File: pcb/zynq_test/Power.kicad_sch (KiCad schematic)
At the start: 83 parts, among them J1401 Barrel_Jack, J1402 Conn_02x04_Odd_Even, Q1104 2N7002E, SW1401 Enable, U1401 LM65645RZT, U1402 LM65645RZT, U1403 LM65645RZT, U1404 LM65645RZT, U1405 74LVC1G17, U1406 TPS259470x

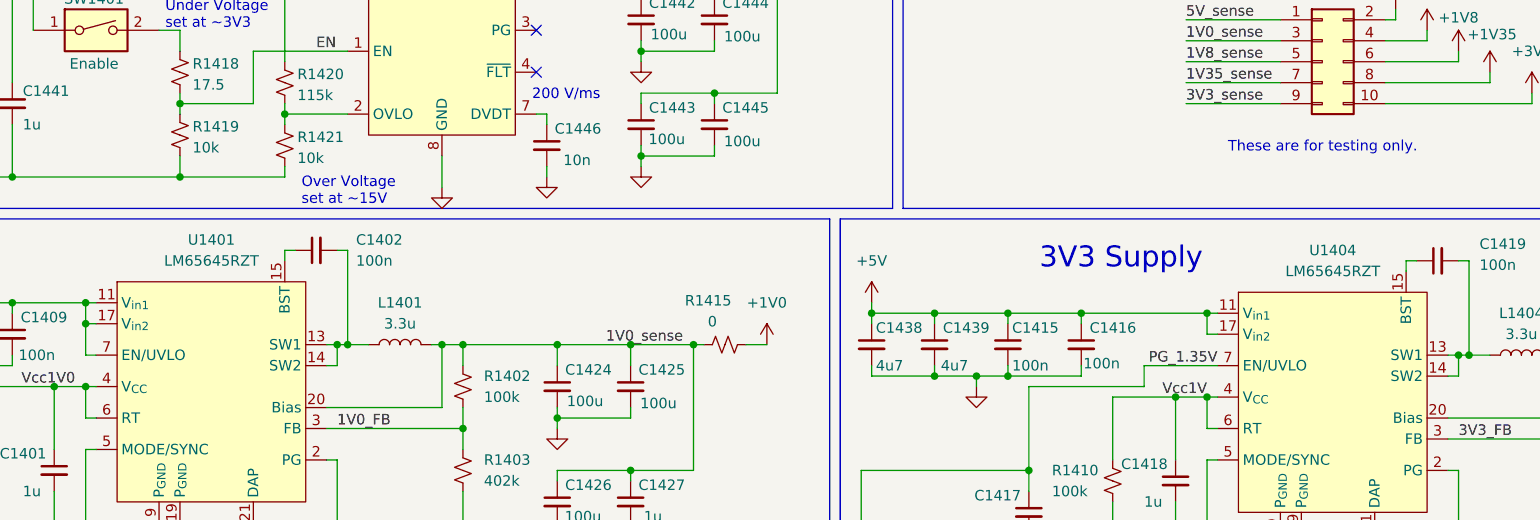
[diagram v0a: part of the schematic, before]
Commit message: Finished most of the schematic, will start routing soon
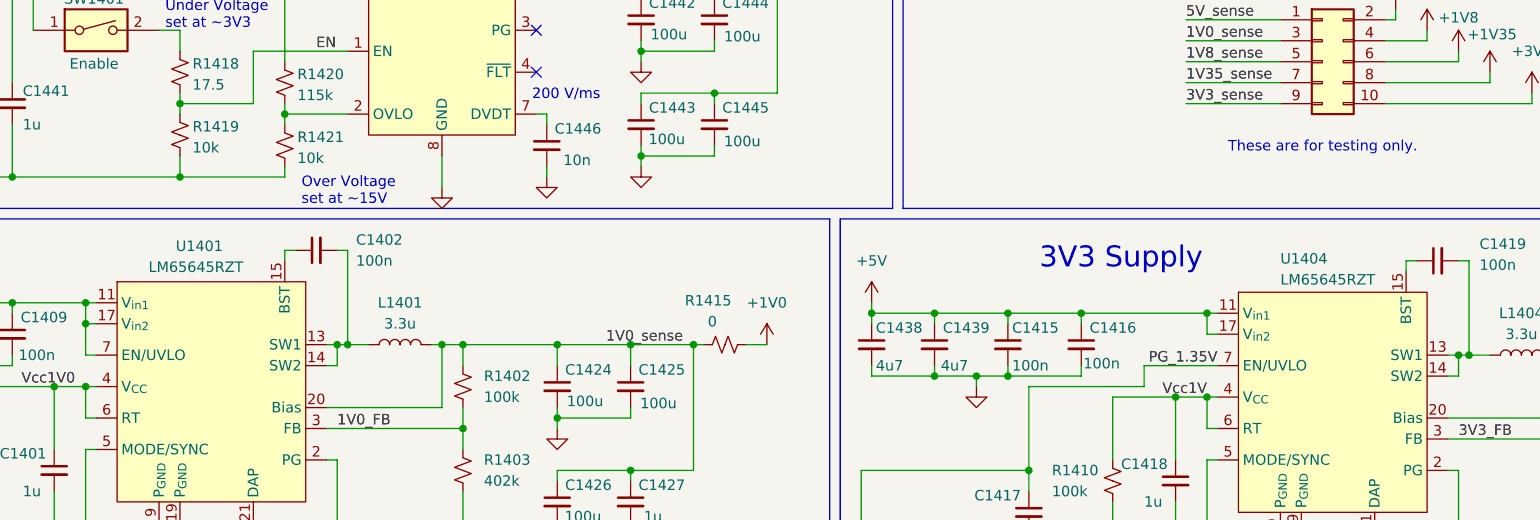
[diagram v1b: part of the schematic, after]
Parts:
- J1401: footprint (none) -> Connector_BarrelJack:BarrelJack_GCT_DCJ200-10-A_Horizontal
- J1402: value Conn_02x04_Odd_Even -> Conn_02x05_Odd_Even; footprint (none) -> Connector_PinSocket_2.54mm:PinSocket_2x05_P2.54mm_Horizontal
- U1405: footprint (none) -> Package_TO_SOT_SMD:Texas_R-PDSO-G5_DCK-5; True values (none) -> SN74LVC1G17DCKR
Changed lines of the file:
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@@
 		(on_board yes)
 		(dnp no)
-		(fields_autoplaced yes)
 		(property "Reference" "U1404"
-			(at 210.82 53.34 0)
-			(effects
-				(font
-					(size 1.27 1.27)
-				)
+			(at 204.47 54.356 0)
+			(effects
+				(font
+					(size 1.27 1.27)
+				)
+				(justify left)
 			)
 		)
 		(property "Value" "LM65645RZT"
-			(at 210.82 55.88 0)
-			(effects
-				(font
-					(size 1.27 1.27)
-				)
+			(at 204.47 56.896 0)
+			(effects
+				(font
+					(size 1.27 1.27)
+				)
+				(justify left)
 			)
 		)
@@
 			)
 		)
-		(property "Footprint" ""
+		(property "Footprint" "Package_TO_SOT_SMD:Texas_R-PDSO-G5_DCK-5"
 			(at 208.28 110.49 0)
 			(effects
@@
 		)
 		(property "Description" "Single Schmitt Buffer Gate, Low-Voltage CMOS"
+			(at 210.82 110.49 0)
+			(effects
+				(font
+					(size 1.27 1.27)
+				)
+				(hide yes)
+			)
+		)
+		(property "True values" "SN74LVC1G17DCKR"
 			(at 210.82 110.49 0)
 			(effects
@@
 		(on_board yes)
 		(dnp no)
-		(fields_autoplaced yes)
 		(property "Reference" "U1401"
-			(at 74.93 52.07 0)
-			(effects
-				(font
-					(size 1.27 1.27)
-				)
+			(at 70.612 52.832 0)
+			(effects
+				(font
+					(size 1.27 1.27)
+				)
+				(justify left)
 			)
 		)
 		(property "Value" "LM65645RZT"
-			(at 74.93 54.61 0)
-			(effects
-				(font
-					(size 1.27 1.27)
-				)
+			(at 67.31 55.372 0)
+			(effects
+				(font
+					(size 1.27 1.27)
+				)
+				(justify left)
 			)
 		)
@@
 			)
 		)
-		(property "Value" "Conn_02x04_Odd_Even"
+		(property "Value" "Conn_02x05_Odd_Even"
 			(at 211.582 22.86 0)
 			(effects
@@
 			)
 		)
-		(property "Footprint" ""
+		(property "Footprint" "Connector_PinSocket_2.54mm:PinSocket_2x05_P2.54mm_Horizontal"
 			(at 209.55 30.48 0)
 			(effects
@@
 			)
 		)
-		(property "Footprint" ""
+		(property "Footprint" "Connector_BarrelJack:BarrelJack_GCT_DCJ200-10-A_Horizontal"
 			(at 38.1 25.146 0)
 			(effects

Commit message: Almost done with BOM
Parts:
- removed R1413, R1414: 0, symbol Device:R_Small_US
- removed SW1401: Enable, symbol Switch:SW_DIP_x01
- added C1447, C1448, C1449, C1450: 10pf, Capacitor_SMD:C_0402_1005Metric, symbol Device:C_Small
- added C1451: 100u, Capacitor_SMD:C_1210_3225Metric, symbol Device:C_Small
- added C1452, C1453, C1454, C1455, C1456: 2.2n, Capacitor_SMD:C_0402_1005Metric, symbol Device:C_Small
- added R1414: 787R, Resistor_SMD:R_0402_1005Metric, symbol Device:R_US
- added R1416: 1k, Resistor_SMD:R_0402_1005Metric, symbol Device:R_Small_US
- added SW1401: Enable, Button_Switch_THT:SW_Slide-03_Wuerth-WS-SLTV_10x2.5x6.4_P2.54mm, symbol Switch:SW_SPDT_321
- C1401: renamed from C1434; footprint (none) -> Capacitor_SMD:C_0805_2012Metric
- C1402: renamed from C1436; footprint (none) -> Capacitor_SMD:C_0805_2012Metric
- C1403: renamed from C1432; footprint (none) -> Capacitor_SMD:C_0805_2012Metric
- C1404: renamed from C1435; footprint (none) -> Capacitor_SMD:C_0805_2012Metric
- C1405: renamed from C1437; footprint (none) -> Capacitor_SMD:C_0805_2012Metric
- C1406: renamed from C1433; footprint (none) -> Capacitor_SMD:C_0805_2012Metric
- C1407: renamed from C1411; footprint (none) -> Capacitor_SMD:C_0402_1005Metric
- C1408: renamed from C1413; footprint (none) -> Capacitor_SMD:C_0402_1005Metric
- C1409: renamed from C1410; footprint (none) -> Capacitor_SMD:C_0402_1005Metric
- C1410: renamed from C1408; footprint (none) -> Capacitor_SMD:C_0402_1005Metric
- C1411: renamed from C1412; footprint (none) -> Capacitor_SMD:C_0402_1005Metric
- C1412: renamed from C1407; footprint (none) -> Capacitor_SMD:C_0402_1005Metric
- C1413: renamed from C1414; footprint (none) -> Capacitor_SMD:C_0402_1005Metric
- C1414: renamed from C1441; footprint (none) -> Capacitor_SMD:C_0805_2012Metric
- C1415: renamed from C1409; footprint (none) -> Capacitor_SMD:C_0402_1005Metric
- C1416: renamed from C1401; footprint (none) -> Capacitor_SMD:C_0805_2012Metric
- C1417: renamed from C1405; footprint (none) -> Capacitor_SMD:C_0805_2012Metric
- C1418: renamed from C1403; footprint (none) -> Capacitor_SMD:C_0805_2012Metric
- C1419: renamed from C1402; footprint (none) -> Capacitor_SMD:C_0402_1005Metric
- C1420: renamed from C1406; footprint (none) -> Capacitor_SMD:C_0402_1005Metric
- C1421: renamed from C1404; footprint (none) -> Capacitor_SMD:C_0402_1005Metric
- C1422: renamed from C1446; footprint (none) -> Capacitor_SMD:C_0402_1005Metric
- C1423: renamed from C1424; footprint (none) -> Capacitor_SMD:C_1210_3225Metric
- C1424: renamed from C1426; footprint (none) -> Capacitor_SMD:C_1210_3225Metric
- C1425: renamed from C1420; footprint (none) -> Capacitor_SMD:C_0805_2012Metric
- C1426: renamed from C1425; value 100u -> 1u; footprint (none) -> Capacitor_SMD:C_0805_2012Metric
- C1427: footprint (none) -> Capacitor_SMD:C_0805_2012Metric
- C1428: renamed from C1442; footprint (none) -> Capacitor_SMD:C_1210_3225Metric
- C1429: renamed from C1443; footprint (none) -> Capacitor_SMD:C_1210_3225Metric
- C1430: renamed from C1422; footprint (none) -> Capacitor_SMD:C_0805_2012Metric
- C1431: renamed from C1421; footprint (none) -> Capacitor_SMD:C_0805_2012Metric
- C1432: renamed from C1444; footprint (none) -> Capacitor_SMD:C_1210_3225Metric
- C1433: renamed from C1445; footprint (none) -> Capacitor_SMD:C_1210_3225Metric
- C1434: renamed from C1423; footprint (none) -> Capacitor_SMD:C_0805_2012Metric
- C1435: renamed from C1438; footprint (none) -> Capacitor_SMD:C_0805_2012Metric
- C1436: renamed from C1439; footprint (none) -> Capacitor_SMD:C_0805_2012Metric
- C1437: renamed from C1415; footprint (none) -> Capacitor_SMD:C_0402_1005Metric
- C1438: renamed from C1417; footprint (none) -> Capacitor_SMD:C_0402_1005Metric
- C1439: renamed from C1416; footprint (none) -> Capacitor_SMD:C_0402_1005Metric
- C1440: footprint (none) -> Capacitor_SMD:C_0402_1005Metric
- C1441: renamed from C1418; footprint (none) -> Capacitor_SMD:C_0805_2012Metric
- C1442: renamed from C1419; footprint (none) -> Capacitor_SMD:C_0402_1005Metric
- C1443: renamed from C1428; footprint (none) -> Capacitor_SMD:C_1210_3225Metric
- C1444: renamed from C1430; footprint (none) -> Capacitor_SMD:C_1210_3225Metric
- C1445: renamed from C1429; footprint (none) -> Capacitor_SMD:C_1210_3225Metric
- C1446: renamed from C1431; footprint (none) -> Capacitor_SMD:C_0805_2012Metric
- D1401: footprint (none) -> LED_SMD:LED_0805_2012Metric
- L1401, L1404: footprint (none) -> Inductor_SMD:L_Bourns_SRP5030T
- L1402: renamed from L1403; footprint (none) -> Inductor_SMD:L_Bourns_SRP5030T
- L1403: renamed from L1402; value 3.3u -> 1.5u; footprint (none) -> Inductor_SMD:L_Bourns_SRP5030T
- R1401: footprint (none) -> Resistor_SMD:R_0402_1005Metric
- R1402: renamed from R1407; footprint (none) -> Resistor_SMD:R_0402_1005Metric
- R1403: renamed from R1404; footprint (none) -> Resistor_SMD:R_0402_1005Metric
- R1404: renamed from R1418; value 17.5 -> 17.5k; footprint (none) -> Resistor_SMD:R_0402_1005Metric
- R1405: renamed from R1419; footprint (none) -> Resistor_SMD:R_0402_1005Metric
- R1406: renamed from R1420; footprint (none) -> Resistor_SMD:R_0402_1005Metric
- R1407: renamed from R1421; footprint (none) -> Resistor_SMD:R_0402_1005Metric
- R1408: renamed from R1402; footprint (none) -> Resistor_SMD:R_0402_1005Metric
- R1409: renamed from R1403; footprint (none) -> Resistor_SMD:R_0402_1005Metric
- R1410: renamed from R1408; footprint (none) -> Resistor_SMD:R_0402_1005Metric
- R1411: renamed from R1409; footprint (none) -> Resistor_SMD:R_0402_1005Metric
- R1412: renamed from R1405; footprint (none) -> Resistor_SMD:R_0402_1005Metric
- R1413: renamed from R1406; footprint (none) -> Resistor_SMD:R_0402_1005Metric
- R1415: value 0 -> 1k; footprint (none) -> Resistor_SMD:R_0402_1005Metric
- R1417, R1422: value 0 -> 787R; footprint (none) -> Resistor_SMD:R_0402_1005Metric
- R1418: renamed from R1410; footprint (none) -> Resistor_SMD:R_0402_1005Metric
- R1419: renamed from R1411; footprint (none) -> Resistor_SMD:R_0402_1005Metric
- R1420: renamed from R1412; footprint (none) -> Resistor_SMD:R_0402_1005Metric
- R1421: renamed from R1416; value 220 -> 220R; footprint (none) -> Resistor_SMD:R_0402_1005Metric
- U1401: footprint (none) -> other:RZT0020A-MFG
- U1402: renamed from U1403; footprint (none) -> other:RZT0020A-MFG
- U1403: renamed from U1402; footprint (none) -> other:RZT0020A-MFG
- U1404: renamed from U1406; value TPS259470x -> TPS259470L; footprint (none) -> other:VQFN-HR-1
- U1405: renamed from U1404; footprint (none) -> other:RZT0020A-MFG
- renumbered Q1104 to Q1401, U1405 to U1406
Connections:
- net +1V0: now also C1423.1, C1424.1, C1426.1, C1427.1, J1402.8 (Pin_8), L1401.2, R1408.1, U1401.20 (Bias), C1448.1, C1456.2; no longer J1402.4 (Pin_4), R1415.2
- net +1V35: now also C1425.1, C1431.1, J1402.6 (Pin_6), L1402.2, R1410.1, U1402.20 (Bias), C1450.1, C1454.2; no longer J1402.8 (Pin_8)
- net +1V8: now also C1430.1, C1434.1, J1402.10 (Pin_10), L1403.2, R1412.1, U1403.20 (Bias), C1449.1, C1451.1, C1453.2; no longer J1402.6 (Pin_6)
- net +3V3: now also C1443.1, C1444.1, C1445.1, C1446.1, J1402.4 (Pin_4), L1404.2, R1419.1, U1405.20 (Bias), C1447.1, C1455.2; no longer J1402.10 (Pin_10), R1417.2
- net +5V: now also C1428.1, C1429.1, C1432.1, C1433.1, U1404.6 (OUT); no longer R1422.2
- net 1V0_FB: now also C1448.2
- net 1V0_sense: now also J1402.7 (Pin_7), R1422.2, C1456.1; no longer C1423.1, C1424.1, C1426.1, C1427.1, J1402.3 (Pin_3), L1401.2, R1408.1, R1415.1, U1401.20 (Bias)
- net 1V35_FB: now also C1450.2
- net 1V35_sense: now also J1402.5 (Pin_5), C1454.1, R1416.2; no longer C1425.1, C1431.1, J1402.7 (Pin_7), L1402.2, R1410.1, U1402.20 (Bias)
- net 1V8_FB: now also C1449.2
- net 1V8_sense: now also J1402.9 (Pin_9), R1415.2, C1453.1; no longer C1430.1, C1434.1, J1402.5 (Pin_5), L1403.2, R1412.1, U1403.20 (Bias)
- net 3V3_FB: now also C1447.2
- net 3V3_sense: now also J1402.3 (Pin_3), R1417.2, C1455.1; no longer C1443.1, C1444.1, C1445.1, C1446.1, J1402.9 (Pin_9), L1404.2, R1417.1, R1419.1, U1405.20 (Bias)
- net GND: now also J1401.3, J1402.1 (Pin_1), C1451.2, C1452.2, R1414.2, SW1401.3 (A)
- net V_{in}: now also SW1401.2 (B)
- net at C1419.2, L1401.1, U1401.13 (SW1)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: now also R1422.1
- net at C1442.2, L1404.1, U1405.13 (SW1)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: now also R1417.1
- net at C1420.2, L1402.1, U1402.13 (SW1)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: now also R1416.1
- net at C1421.2, L1403.1, U1403.13 (SW1)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: now also R1415.1
- net at R1404.1: now also SW1401.1 (C)
- removed net 5V_sense: C1428.1, C1429.1, C1432.1, C1433.1, J1402.1 (Pin_1), R1422.1, U1404.6 (OUT)
- new net: R1414.1, U1404.9 (ILM)
- new net: C1452.1, U1404.10 (ITIMER)
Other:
- note added: "I_{lim} set at 4.3A"
- note added: "SRP3012TA-1R5M"
- note removed: "These are for testing only."
- moved on the sheet: C1414, C1423, C1424, C1425, C1426, C1427, C1428, C1429, C1430, C1431, C1432, C1433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

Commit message: Version sent to JLCPCB
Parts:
- added C1457, C1458: 100n, Capacitor_SMD:C_0402_1005Metric, symbol Device:C_Small
- added R1423: 45.3k, Resistor_SMD:R_0402_1005Metric, symbol Device:R_Small_US
- added R1424: 249k, Resistor_SMD:R_0402_1005Metric, symbol Device:R_Small_US
- added R1425, R1426, R1427, R1428: 0R, Resistor_SMD:R_0402_1005Metric, symbol Device:R_Small_US
- added R1429: 0R, Resistor_SMD:R_0402_1005Metric, symbol Device:R_US
- added R1430, R1431: 10k, Resistor_SMD:R_0402_1005Metric, symbol Device:R_Small_US
- added U1407, U1408: LTC6908-1, Package_TO_SOT_SMD:TSOT-23-6, symbol other:LTC6908-1
- C1401, C1402, C1403, C1404, C1405, C1406, C1431, C1434, C1435, C1436: JLCPCB Part# (none) -> C1779; PART_NUMBER (none) -> CL21A475KAQNNNE
- C1407, C1408, C1409, C1410, C1411, C1412, C1413, C1415, C1419, C1420, C1421, C1437, C1438, C1439, C1442: JLCPCB Part# (none) -> C1525; PART_NUMBER (none) -> CL05B104KO5NNNC
- C1414, C1416, C1417, C1418, C1425, C1426, C1427, C1430, C1441, C1446: JLCPCB Part# (none) -> C28323; PART_NUMBER (none) -> CL21B105KBFNNNE
- C1422: JLCPCB Part# (none) -> C77013; PART_NUMBER (none) -> GRM155R71E103KA01D
- C1423, C1424, C1428, C1429, C1432, C1433, C1443, C1444, C1445, C1451: JLCPCB Part# (none) -> C23742; PART_NUMBER (none) -> CL32A107MPVNNNE
- C1440: JLCPCB Part# (none) -> C23733; PART_NUMBER (none) -> CL05A475MP5NRNC
- C1447, C1448, C1449, C1450: JLCPCB Part# (none) -> C32949; PART_NUMBER (none) -> CL05C100JB5NNNC
- C1452, C1453, C1454, C1455, C1456: JLCPCB Part# (none) -> C1531; PART_NUMBER (none) -> 0402B222K500NT
- D1401: JLCPCB Part# (none) -> C84256; PART_NUMBER (none) -> NCD0805R1
- J1401: JLCPCB Part# (none) -> C5280493; PART_NUMBER (none) -> DCJ200-10-A-K1-K
- J1402: now left out of the parts list
- L1401, L1404: JLCPCB Part# (none) -> C2047182; PART_NUMBER (none) -> SRP3012TA-3R3M
- L1402, L1403: JLCPCB Part# (none) -> C2052178; PART_NUMBER (none) -> SRP3012TA-1R5M
- Q1401: JLCPCB Part# (none) -> C71533; PART_NUMBER (none) -> 2N7002E
- R1401, R1402, R1403, R1408, R1410, R1412, R1418, R1419: JLCPCB Part# (none) -> C192169; PART_NUMBER (none) -> ERJ2RKF1003X
- R1404: JLCPCB Part# (none) -> C129766; PART_NUMBER (none) -> 0402WGF1782TCE
- R1405, R1407: JLCPCB Part# (none) -> C191123; PART_NUMBER (none) -> ERJ2RKF1002X
- R1406: JLCPCB Part# (none) -> C2077118; PART_NUMBER (none) -> ERJ2RKF1153X
- R1409: JLCPCB Part# (none) -> C2076841; PART_NUMBER (none) -> ERJ2RKF4023X
- R1411: value 145k -> 143k; JLCPCB Part# (none) -> C5197520; PART_NUMBER (none) -> RT0402BRD07147KL
- R1413: JLCPCB Part# (none) -> C416576; PART_NUMBER (none) -> ERJ2RKF8062X
- R1414, R1417, R1422: JLCPCB Part# (none) -> C2077114; PART_NUMBER (none) -> ERJ2RKF7870X
- R1415, R1416: JLCPCB Part# (none) -> C242161; PART_NUMBER (none) -> ERJ2RKF1001X
- R1420: value 145k -> 31.6k; JLCPCB Part# (none) -> C2986236; PART_NUMBER (none) -> ERJ2RKF3162X
- R1421: JLCPCB Part# (none) -> C412979; PART_NUMBER (none) -> ERJ2GEJ221X
- SW1401: JLCPCB Part# (none) -> C5362723; PART_NUMBER (none) -> 450301014042
- U1401, U1402, U1403, U1405: JLCPCB Part# (none) -> C49256229; PART_NUMBER (none) -> LM65645RZTR
- U1404: JLCPCB Part# (none) -> C3662793; PART_NUMBER (none) -> TPS259470LRPWR
- U1406: JLCPCB Part# (none) -> C10425; PART_NUMBER (none) -> SN74LVC1G17DCKR
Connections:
- net +3V3: now also R1430.1
- net +5V: now also C1457.1, C1458.1, R1423.1, R1424.1, U1407.1 (Vin), U1408.1 (Vin)
- net GND: now also C1457.2, C1458.2, R1431.2, U1407.2 (GND), U1407.4 (MOD), U1408.2 (GND), U1408.4 (MOD); no longer U1401.5 (MODE/SYNC), U1402.5 (MODE/SYNC), U1403.5 (MODE/SYNC), U1405.5 (MODE/SYNC)
- net PWR_ON_RST: now also R1429.2, R1430.2, R1431.1; no longer U1406.4
- new net: R1424.2, U1408.3 (SET)
- new net: R1428.1, U1408.5 (OUT2)
- new net: R1427.1, U1408.6 (OUT1)
- new net: R1423.2, U1407.3 (SET)
- new net: R1426.1, U1407.5 (OUT2)
- new net: R1425.1, U1407.6 (OUT1)
- new net: R1429.1, U1406.4
- new net 2.2MHz_Sync: R1425.2, U1403.5 (MODE/SYNC)
- new net 400kHz_Sync: R1427.2, U1401.5 (MODE/SYNC)
- new net ~{2.2MHz_Sync}: R1426.2, U1402.5 (MODE/SYNC)
- new net ~{400kHz_Sync}: R1428.2, U1405.5 (MODE/SYNC)
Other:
- note added: "CLK SYNC"
- note removed: "SRP3012TA-1R5M"
- moved on the sheet: C1401, C1402, C1403, C1404, C1405, C1406, C1407, C1408, C1409, C1410, C1411, C1412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
